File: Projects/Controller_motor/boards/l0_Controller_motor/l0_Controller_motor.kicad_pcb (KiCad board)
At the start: 2 copper layers, 20.3 x 15.2 mm, 12 parts, among them J1 l0_Socket, J2 Header6Contacts, U1 MC33926

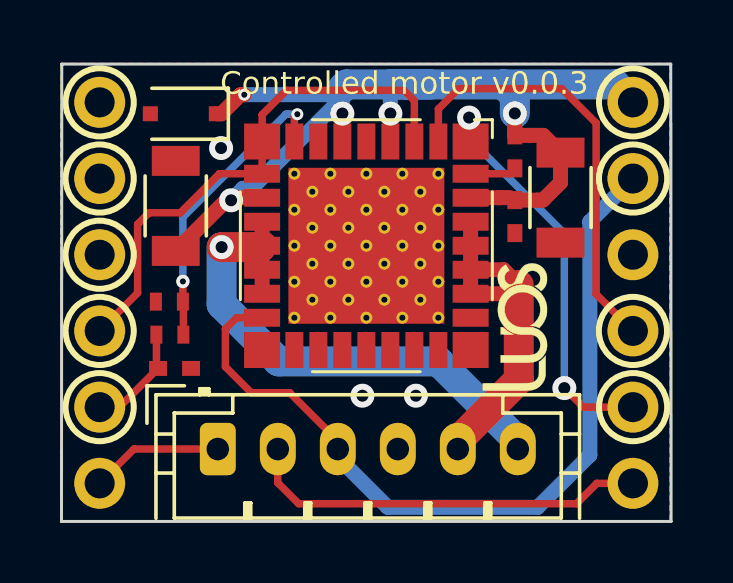
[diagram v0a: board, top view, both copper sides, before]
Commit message: Rename "controlled motor" to "controller motor" in every existing occurences of Examples
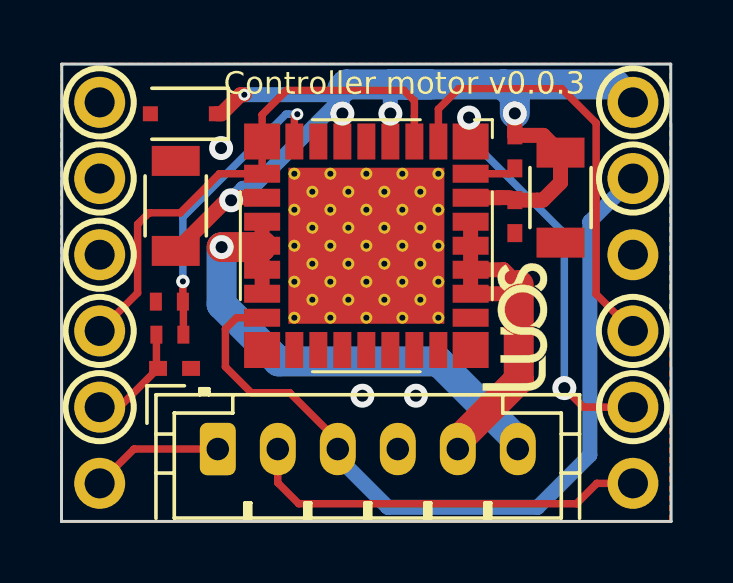
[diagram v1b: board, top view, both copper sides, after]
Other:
- board text added: "Controller motor v0.0.3"
- board text removed: "Controlled motor v0.0.3"
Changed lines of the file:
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@@
       (drillshape 0)
       (scaleselection 1)
-      (outputdirectory "Controlled_motor_v0.0.2/"))
+      (outputdirectory "Controller_motor_v0.0.2/"))
   )
   (net 0 "")
@@
     (arrow2b (pts (xy 125.932198 76.531813) (xy 127.060527 75.948911)))
   )
-  (gr_text "Controlled motor v0.0.3" (at 137.397501 82.170001) (layer F.SilkS)
+  (gr_text "Controller motor v0.0.3" (at 137.397501 82.170001) (layer F.SilkS)
     (effects (font (size 0.75 0.75) (thickness 0.1875)))
   )
